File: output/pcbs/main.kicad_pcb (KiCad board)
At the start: 2 copper layers, 110.4 x 89 mm, 84 parts, among them Q1 AO3400A, SW1 CPG1316S01D02_reversible, SW10 CPG1316S01D02_reversible, SW11 CPG1316S01D02_reversible, SW12 CPG1316S01D02_reversible, SW13 CPG1316S01D02_reversible, SW14 CPG1316S01D02_reversible, SW15 CPG1316S01D02_reversible, SW16 CPG1316S01D02_reversible, SW17 CPG1316S01D02_reversible, SW18 CPG1316S01D02_reversible, SW2 CPG1316S01D02_reversible, SW3 CPG1316S01D02_reversible, SW4 CPG1316S01D02_reversible, SW5 CPG1316S01D02_reversible, SW6 CPG1316S01D02_reversible, SW7 CPG1316S01D02_reversible, SW8 CPG1316S01D02_reversible, SW9 CPG1316S01D02_reversible

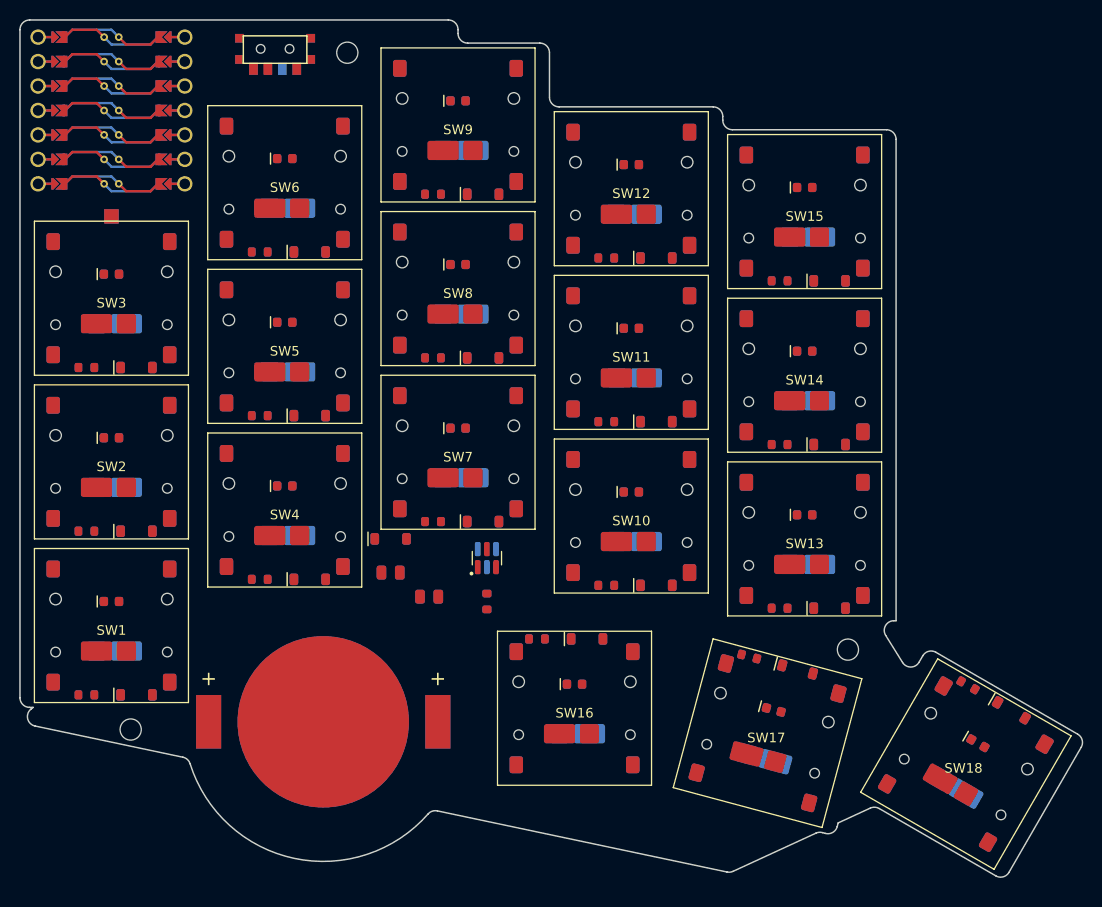
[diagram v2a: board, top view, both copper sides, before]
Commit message: Draw the board outline as one straight-edged polygon
The outline was the union of the key rectangles, the XIAO strip, the
coin-cell circle and a bottom polygon: a stepped top edge, a round bulge
under the CR2032 and small notches, with 1 mm fillets. It is now a single
8-sided polygon with 3 mm rounded corners: flat top over the XIAO and power
switch, a diagonal down to the inner column, a straight right edge, one
notch for the outer thumb key and a straight bottom tangent under the coin
cell. output/ is the regenerated ergogen output.

Co-Authored-By: Claude Opus 5.5 (1M context) <noreply@anthropic.com>
Claude-Session: https://claude.ai/code/session_0165D9fBjcdWGjdLPuN9BjoD
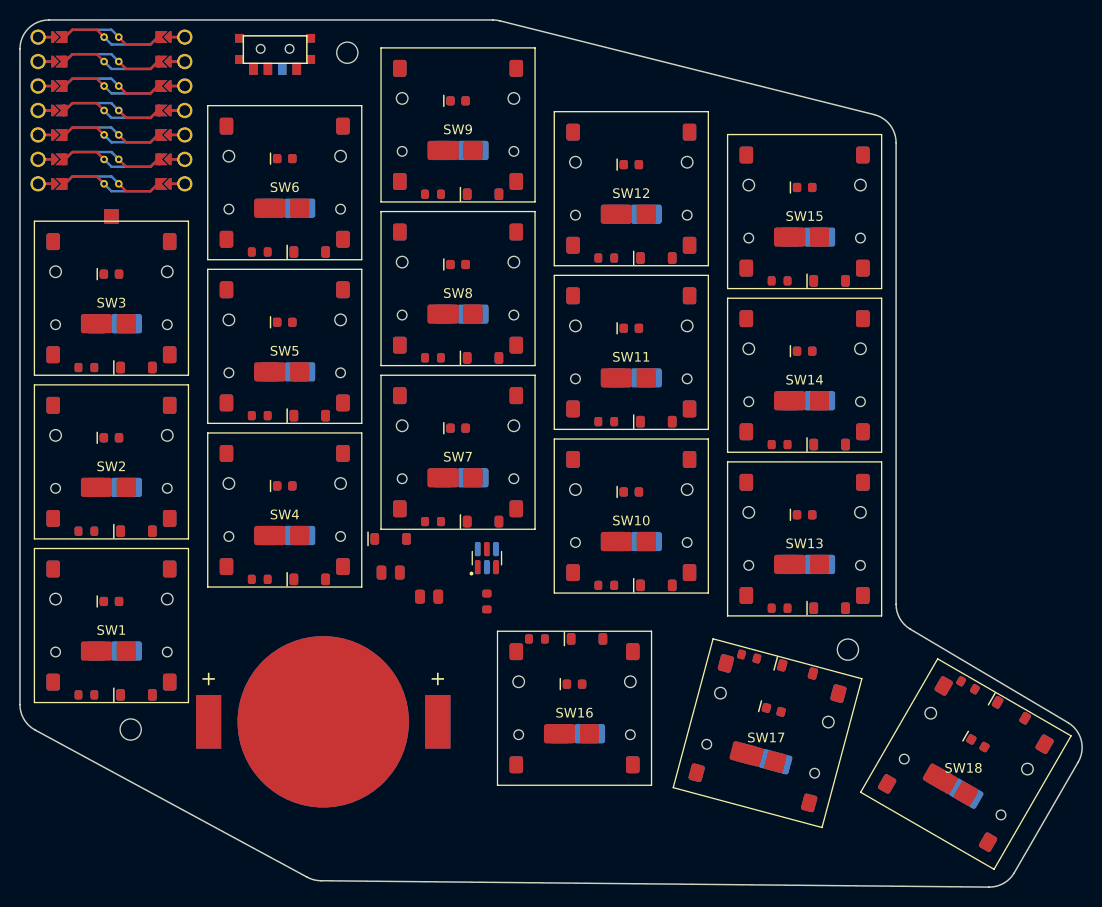
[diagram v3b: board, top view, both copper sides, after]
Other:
- board size 110.4 x 89 mm -> 110.3 x 90.1 mm
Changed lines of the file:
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@@
       (pad "" np_thru_hole circle (at 0 0) (size 2.2 2.2) (drill 2.2) (layers *.Cu *.Mask))
     )
-            (gr_line (start -8.5 8.5) (end -8.13138686131387 8.5) (angle 90) (layer Edge.Cuts) (width 0.15))
-(gr_line (start -9.5 7.5) (end -9.5 -61.9) (angle 90) (layer Edge.Cuts) (width 0.15))
-(gr_line (start 45.5 -54.875) (end 45.5 -59.5) (angle 90) (layer Edge.Cuts) (width 0.15))
-(gr_line (start 44.5 -60.5) (end 37 -60.5) (angle 90) (layer Edge.Cuts) (width 0.15))
-(gr_line (start 63.5 -52.5) (end 63.5 -52.875) (angle 90) (layer Edge.Cuts) (width 0.15))
-(gr_line (start 62.5 -53.875) (end 46.5 -53.875) (angle 90) (layer Edge.Cuts) (width 0.15))
-(gr_line (start 81.2727050344033 -0.5) (end 81.5 -0.5) (angle 90) (layer Edge.Cuts) (width 0.15))
-(gr_line (start 81.5 -0.5) (end 81.5 -50.5) (angle 90) (layer Edge.Cuts) (width 0.15))
-(gr_line (start 80.5 -51.5) (end 64.5 -51.5) (angle 90) (layer Edge.Cuts) (width 0.15))
-(gr_line (start 73.85211255029765 21.50772402256877) (end 74.16040774114451 21.59033147070751) (angle 90) (layer Edge.Cuts) (width 0.15))
-(gr_line (start 75.38515254114452 20.883224670707477) (end 75.48789128974883 20.499798433954368) (angle 90) (layer Edge.Cuts) (width 0.15))
-(gr_line (start 79.74306498241245 19.004798175076715) (end 91.86121589999999 26.00121589999999) (angle 90) (layer Edge.Cuts) (width 0.15))
-(gr_line (start 93.2272413 25.635190499999993) (end 100.7272413 12.644809500000008) (angle 90) (layer Edge.Cuts) (width 0.15))
-(gr_line (start 100.3612159 11.27878410000001) (end 85.63878410000001 2.77878410000001) (angle 90) (layer Edge.Cuts) (width 0.15))
-(gr_line (start 84.2727587 3.144809500000008) (end 83.88922690186529 3.8091060577846747) (angle 90) (layer Edge.Cuts) (width 0.15))
-(gr_line (start -8.5 -62.9) (end 35 -62.9) (angle 90) (layer Edge.Cuts) (width 0.15))
-(gr_line (start 36 -61.9) (end 36 -61.5) (angle 90) (layer Edge.Cuts) (width 0.15))
-(gr_line (start 63.94365707921543 25.60051830929431) (end 33.85098610437033 19.251613179285403) (angle 90) (layer Edge.Cuts) (width 0.15))
-(gr_line (start 7.421651900261805 13.675593198759085) (end -7.933257315569024 10.43603817812279) (angle 90) (layer Edge.Cuts) (width 0.15))
-(gr_line (start -8.352817615569025 8.677750078122791) (end -8.13138686131387 8.5) (angle 90) (layer Edge.Cuts) (width 0.15))
-(gr_line (start 80.42400213440328 1.0288698999999895) (end 82.17449860186527 3.837975957784664) (angle 90) (layer Edge.Cuts) (width 0.15))
-(gr_line (start 73.17486635029766 21.565399422568774) (end 64.56851837921542 25.53030820929432) (angle 90) (layer Edge.Cuts) (width 0.15))
-(gr_line (start 78.82463778241247 18.962573175076706) (end 75.48789128974883 20.499798433954318) (angle 90) (layer Edge.Cuts) (width 0.15))
-(gr_arc (start 22 10) (end 8.1690747 14.353792200000001) (angle -121.22645267614644) (layer Edge.Cuts) (width 0.15))
-(gr_arc (start -7.726823215569024 9.457577678122792) (end -8.352817615569025 8.677750078122791) (angle -129.3313278037844) (layer Edge.Cuts) (width 0.15))
-(gr_arc (start 7.2152178 14.6540537) (end 8.1690747 14.353792200000001) (angle -60.61322531882978) (layer Edge.Cuts) (width 0.15))
-(gr_arc (start 33.644552 20.2300737) (end 33.8509861 19.251613199999998) (angle -60.613227357316546) (layer Edge.Cuts) (width 0.15))
-(gr_arc (start 64.15009117921544 24.62205780929431) (end 63.943657079215434 25.600518309294312) (angle -36.64879121326868) (layer Edge.Cuts) (width 0.15))
-(gr_arc (start 73.59329355029764 22.47364982256878) (end 73.85211255029765 21.50772402256878) (angle -39.73532624091183) (layer Edge.Cuts) (width 0.15))
-(gr_arc (start 74.41922674114451 20.62440567070751) (end 74.16040774114451 21.59033147070751) (angle -90.0000000000021) (layer Edge.Cuts) (width 0.15))
-(gr_arc (start 79.24306498241245 19.870823575076713) (end 79.74306498241245 19.00479817507671) (angle -54.73532845561144) (layer Edge.Cuts) (width 0.15))
-(gr_arc (start 92.36121589999999 25.13519049999999) (end 91.86121589999999 26.00121589999999) (angle -90.00000000000011) (layer Edge.Cuts) (width 0.15))
-(gr_arc (start 99.8612159 12.144809500000008) (end 100.7272413 12.644809500000008) (angle -89.99999999999996) (layer Edge.Cuts) (width 0.15))
-(gr_arc (start 85.1387841 3.644809500000001) (end 85.6387841 2.778784100000001) (angle -90.00000000000128) (layer Edge.Cuts) (width 0.15))
-(gr_arc (start 83.02320150186529 3.3091060577846747) (end 82.17449860186528 3.837975957784675) (angle -118.07086931838666) (layer Edge.Cuts) (width 0.15))
-(gr_arc (start 81.2727050344033 0.5) (end 81.2727050344033 -0.5) (angle -121.92913057319714) (layer Edge.Cuts) (width 0.15))
-(gr_arc (start 80.5 -50.5) (end 81.5 -50.5) (angle -90) (layer Edge.Cuts) (width 0.15))
-(gr_arc (start 64.5 -52.5) (end 63.5 -52.5) (angle -90) (layer Edge.Cuts) (width 0.15))
-(gr_arc (start 62.5 -52.875) (end 63.5 -52.875) (angle -90) (layer Edge.Cuts) (width 0.15))
-(gr_arc (start 46.5 -54.875) (end 45.5 -54.875) (angle -90) (layer Edge.Cuts) (width 0.15))
-(gr_arc (start 44.5 -59.5) (end 45.5 -59.5) (angle -90) (layer Edge.Cuts) (width 0.15))
-(gr_arc (start 37 -61.5) (end 36 -61.5) (angle -90) (layer Edge.Cuts) (width 0.15))
-(gr_arc (start 35 -61.9) (end 36 -61.9) (angle -90) (layer Edge.Cuts) (width 0.15))
-(gr_arc (start -8.5 -61.9) (end -8.5 -62.9) (angle -90) (layer Edge.Cuts) (width 0.15))
-(gr_arc (start -8.5 7.5) (end -9.5 7.5) (angle -90) (layer Edge.Cuts) (width 0.15))
+            (gr_line (start -9.5 8.212090332786886) (end -9.5 -59.9) (angle 90) (layer Edge.Cuts) (width 0.15))
+(gr_line (start -6.5 -62.9) (end 39.62981965576927 -62.9) (angle 90) (layer Edge.Cuts) (width 0.15))
+(gr_line (start 40.35907642628079 -62.810014582329636) (end 79.22925677051151 -53.06905372498025) (angle 90) (layer Edge.Cuts) (width 0.15))
+(gr_line (start 81.5 -50.159039142650606) (end 81.5 -2.209354106013187) (angle 90) (layer Edge.Cuts) (width 0.15))
+(gr_line (start 82.97051743014832 0.37147581185367073) (end 99.358642162515 10.083604354565267) (angle 90) (layer Edge.Cuts) (width 0.15))
+(gr_line (start 100.42723579266328 14.164434272432118) (end 93.78582043049865 25.667703063601664) (angle 90) (layer Edge.Cuts) (width 0.15))
+(gr_line (start 91.15920042954721 27.167567263592595) (end 21.74426707400716 26.50708172742755) (angle 90) (layer Edge.Cuts) (width 0.15))
+(gr_line (start 20.345355033108255 26.14584780479627) (end -7.927455841850316 10.850720610146553) (angle 90) (layer Edge.Cuts) (width 0.15))
+(gr_arc (start -6.5 -59.9) (end -6.5 -62.9) (angle -90) (layer Edge.Cuts) (width 0.15))
+(gr_arc (start 39.62981965576927 -59.9) (end 40.35907645576927 -62.8100145) (angle -14.068725993539289) (layer Edge.Cuts) (width 0.15))
+(gr_arc (start 78.5 -50.159039142650606) (end 81.5 -50.159039142650606) (angle -75.93127400646087) (layer Edge.Cuts) (width 0.15))
+(gr_arc (start 84.5 -2.209354106013187) (end 81.5 -2.209354106013187) (angle -59.347658154508025) (layer Edge.Cuts) (width 0.15))
+(gr_arc (start 97.8291595926633 12.66443427243211) (end 100.4272357926633 14.16443427243211) (angle -89.34765826292411) (layer Edge.Cuts) (width 0.15))
+(gr_arc (start 91.18774423049865 24.167703063601664) (end 91.15920043049866 27.167567263601665) (angle -60.5451545599808) (layer Edge.Cuts) (width 0.15))
+(gr_arc (start 21.772810874958573 23.507217527436605) (end 20.345355074958572 26.145847827436604) (angle -27.867508757395967) (layer Edge.Cuts) (width 0.15))
+(gr_arc (start -6.5 8.212090332786886) (end -9.5 8.212090332786886) (angle -61.58733657420757) (layer Edge.Cuts) (width 0.15))
 )
